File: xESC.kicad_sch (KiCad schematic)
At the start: 47 parts, among them J18 Conn_01x05, J22 Screw_Terminal_01x03, J36 Conn_02x03_Odd_Even, J39 Screw_Terminal_01x02, J42 Conn_01x02, U10 xESC2, U20 2.54mm 2x2 socket, U23 2.54mm 2x2 socket, U26 2.54mm 2x2 socket, U28 LV2862XDDC, U32 2.54mm 1x6 socket, U35 2.54mm 1x6 socket, U38 2.54mm 1x9 socket, U41 2.54mm 1x5 socket

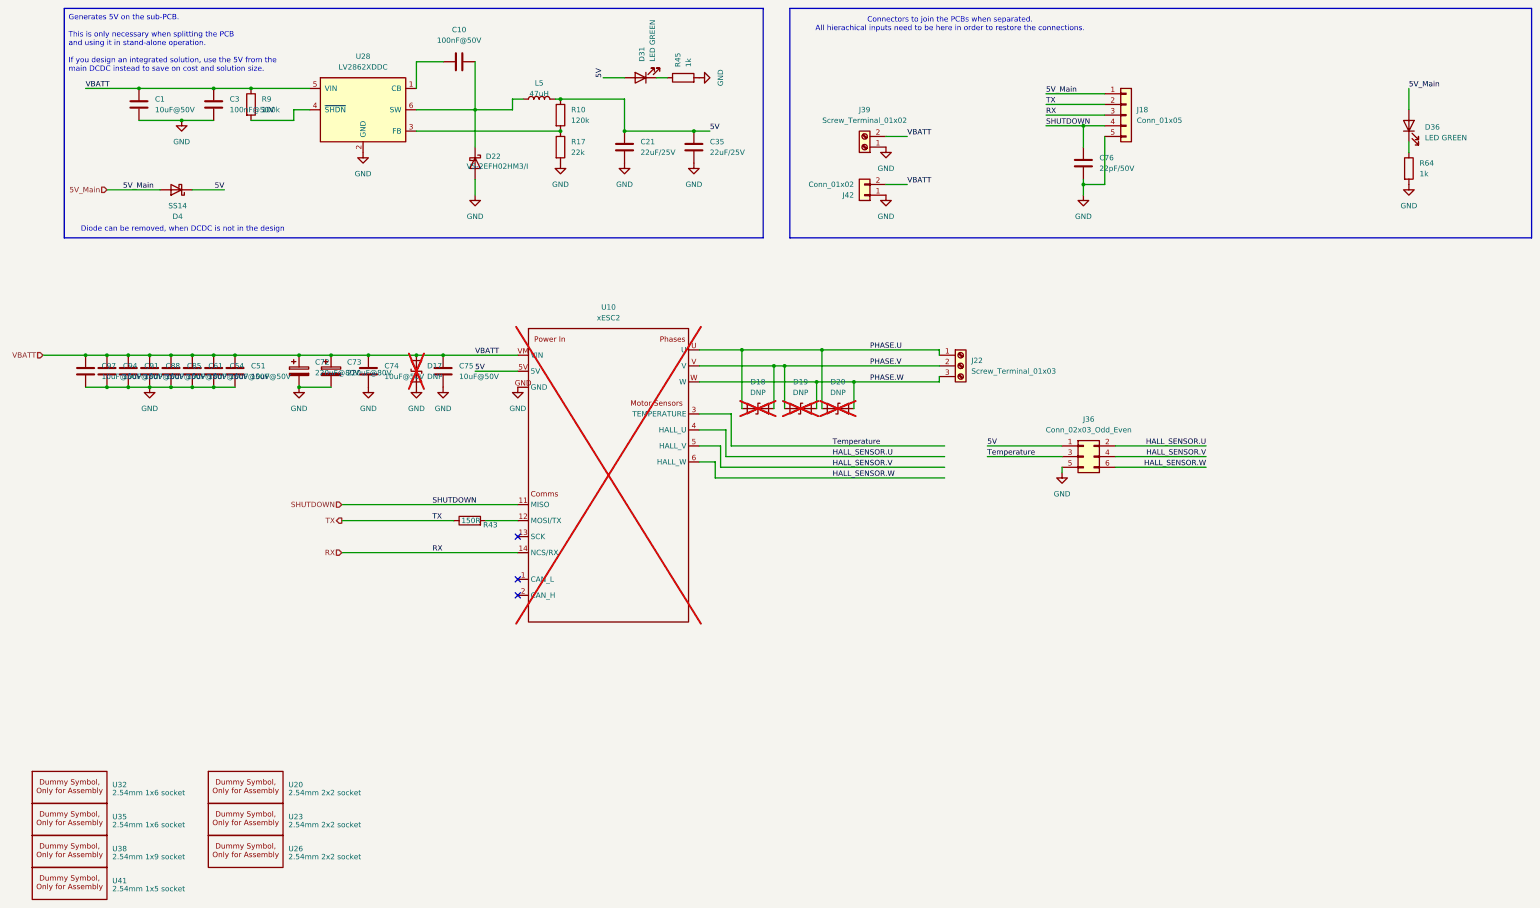
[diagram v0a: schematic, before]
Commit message: New conns for xESC
Added new connectors into the design for motors.
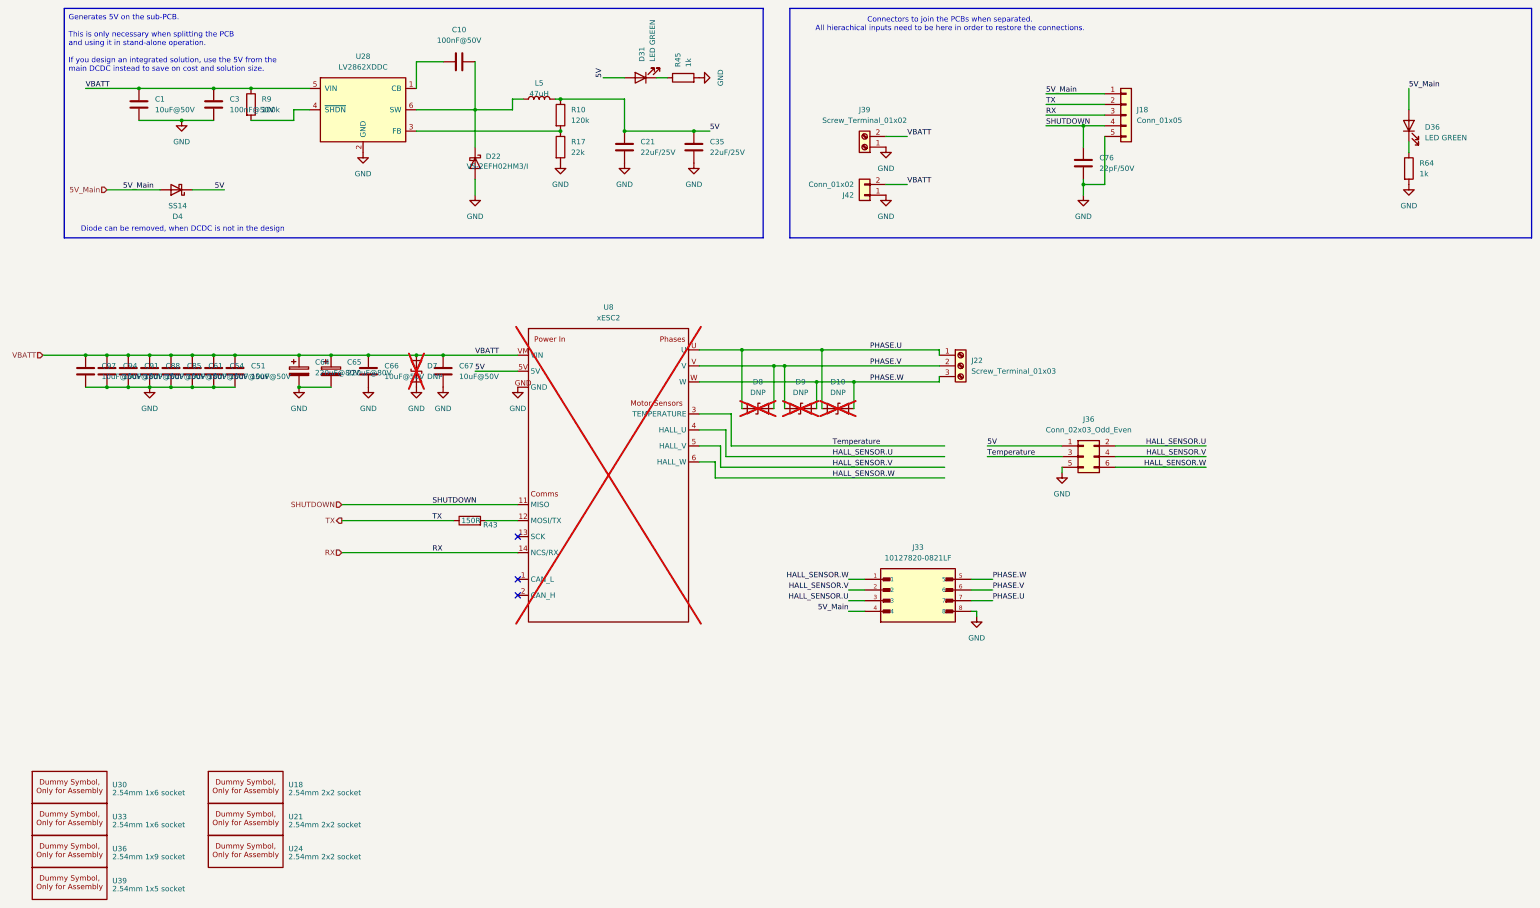
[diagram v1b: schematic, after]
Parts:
- added J33: 10127820-0821LF, 10127820_0821LF:AMPHENOL_10127820-0821LF, symbol 10127820-0821LF:10127820-0821LF
- D22: value VS-2EFH02HM3/I -> VS-2EFH02HM3/I
- renumbered C72 to C64, C73 to C65, C74 to C66, C75 to C67, D20 to D10, D17 to D7, D18 to D8, D19 to D9, U20 to U18, U23 to U21, U26 to U24, U32 to U30, U35 to U33, U38 to U36, U41 to U39, U10 to U8
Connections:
- net 5V_Main: now also J33.4
- net GND: now also J33.8
- net HALL_SENSOR.U: now also J33.3
- net HALL_SENSOR.V: now also J33.2
- net HALL_SENSOR.W: now also J33.1
- net PHASE.U: now also J33.7
- net PHASE.V: now also J33.6
- net PHASE.W: now also J33.5

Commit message: Incremental routing updates
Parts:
- removed J18: Conn_01x05, Connector_JST:JST_XH_B5B-XH-A_1x05_P2.50mm_Vertical, symbol Connector_Generic:Conn_01x05
- removed J39: Screw_Terminal_01x02, TerminalBlock_Phoenix:TerminalBlock_Phoenix_MKDS-1,5-2-5.08_1x02_P5.08mm_Horizontal, symbol Connector:Screw_Terminal_01x02
- removed J42: Conn_01x02, Connector_AMASS:AMASS_XT30U-M_1x02_P5.0mm_Vertical, symbol Connector_Generic:Conn_01x02

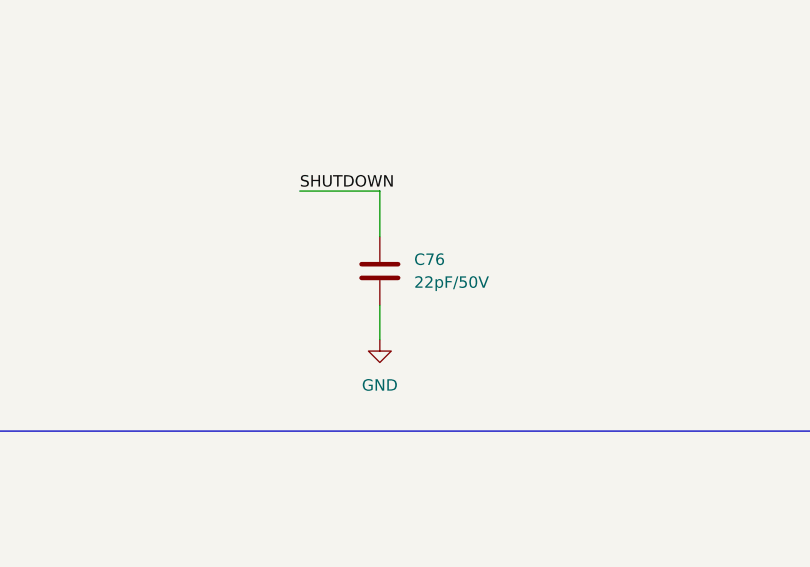
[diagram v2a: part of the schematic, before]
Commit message: Additional routing
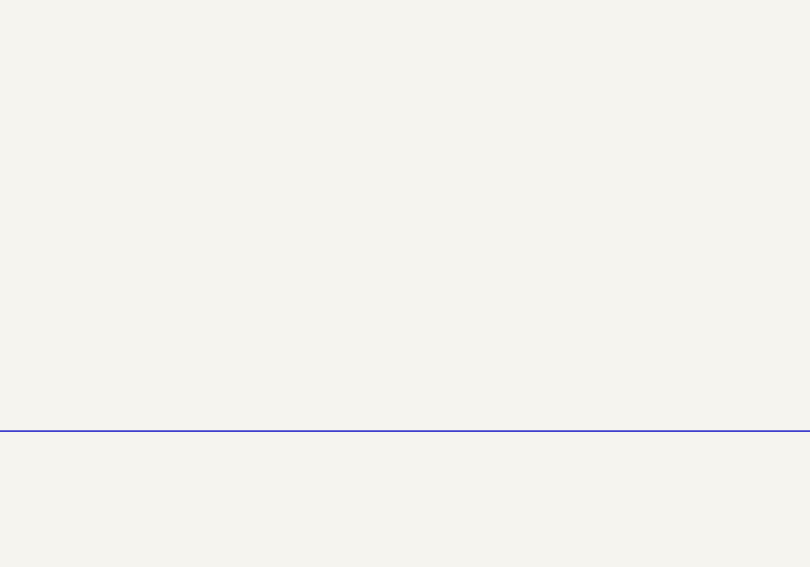
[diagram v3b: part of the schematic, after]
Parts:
- removed C76: 22pF/50V, Capacitor_SMD:C_0603_1608Metric, symbol Device:C

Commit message: Routing progress
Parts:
- D4: now not fitted
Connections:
- net 5V is gone; now on net 5V_Main: C21.1, C35.1, D31.2 (A), D4.1 (K), J36.1 (Pin_1), L5.2, R10.1, U8.5V
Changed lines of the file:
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@@
+	)
+	(junction
+		(at 57.15 60.96)
+		(diameter 0)
+		(color 0 0 0 0)
 	)
 	(junction
@@
 	(junction
 		(at 78.74 36.83)
+		(diameter 0)
+		(color 0 0 0 0)
+	)
+	(junction
+		(at 66.04 60.96)
 		(diameter 0)
 		(color 0 0 0 0)
@@
 	(wire
 		(pts
-			(xy 72.39 60.96) (xy 64.77 60.96)
+			(xy 72.39 60.96) (xy 66.04 60.96)
 		)
 		(stroke
@@
 	(wire
 		(pts
+			(xy 66.04 60.96) (xy 64.77 60.96)
+		)
+		(stroke
+			(width 0)
+			(type default)
+		)
+	)
+	(wire
+		(pts
 			(xy 62.23 44.45) (xy 69.85 44.45)
 		)
@@
 	(wire
 		(pts
+			(xy 57.15 57.15) (xy 66.04 57.15)
+		)
+		(stroke
+			(width 0)
+			(type default)
+		)
+	)
+	(wire
+		(pts
 			(xy 185.42 99.06) (xy 195.58 99.06)
 		)
@@
 	(wire
 		(pts
+			(xy 57.15 60.96) (xy 57.15 57.15)
+		)
+		(stroke
+			(width 0)
+			(type default)
+		)
+	)
+	(wire
+		(pts
 			(xy 132.08 41.91) (xy 132.08 50.8)
 		)
@@
 		(pts
 			(xy 140.97 39.37) (xy 143.51 39.37)
+		)
+		(stroke
+			(width 0)
+			(type default)
+		)
+	)
+	(wire
+		(pts
+			(xy 66.04 57.15) (xy 66.04 60.96)
 		)
 		(stroke
@@
 		(in_bom yes)
 		(on_board yes)
-		(dnp no)
+		(dnp yes)
 		(fields_autoplaced yes)
 		(property "Reference" "D4"

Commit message: Further routing progress
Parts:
- removed D31: LED GREEN, LED_SMD:LED_0805_2012Metric, symbol Device:LED
- removed J22: Screw_Terminal_01x03, TerminalBlock_Phoenix:TerminalBlock_Phoenix_MKDS-1,5-3-5.08_1x03_P5.08mm_Horizontal, symbol Connector:Screw_Terminal_01x03
- removed R45: 1k, Resistor_SMD:R_0805_2012Metric, symbol Device:R

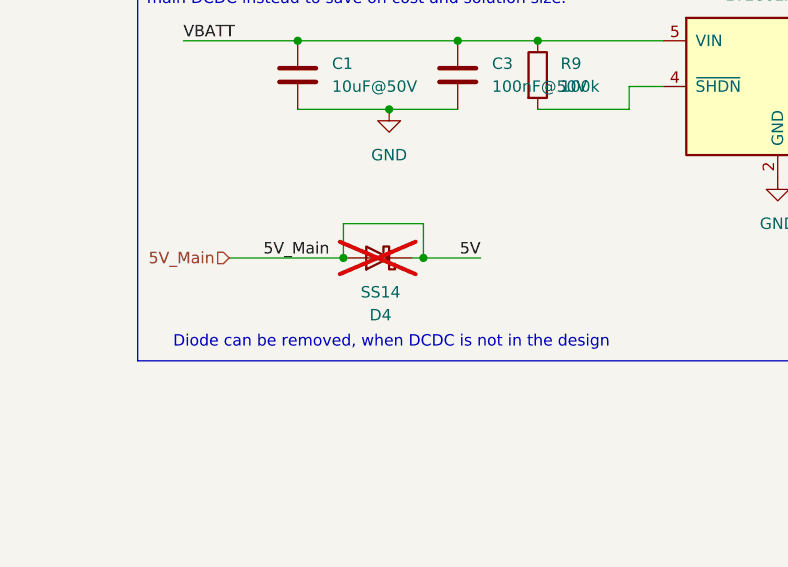
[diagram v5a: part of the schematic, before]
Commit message: Review ready layout
DRC mostly clean.  Need to add GND via stitching and GND return vias yet, and general review
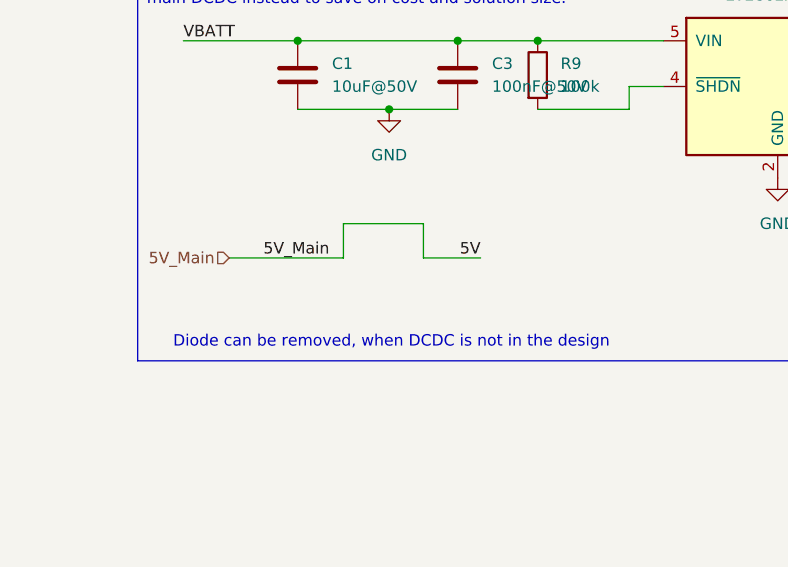
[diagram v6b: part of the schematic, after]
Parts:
- removed D4: SS14, Diode_SMD:D_SMA, symbol Diode:SS14
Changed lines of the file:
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@@
-	)
-	(junction
-		(at 57.15 60.96)
-		(diameter 0)
-		(color 0 0 0 0)
 	)
 	(junction
@@
 	(junction
 		(at 78.74 36.83)
-		(diameter 0)
-		(color 0 0 0 0)
-	)
-	(junction
-		(at 66.04 60.96)
 		(diameter 0)
 		(color 0 0 0 0)
@@
 		(pts
 			(xy 140.97 41.91) (xy 132.08 41.91)
-		)
-		(stroke
-			(width 0)
-			(type default)
-		)
-	)
-	(wire
-		(pts
-			(xy 66.04 60.96) (xy 64.77 60.96)
 		)
 		(stroke
@@
 					(unit 1)
 				)
-			)
-		)
-	)
-	(symbol
-		(lib_id "Diode:SS14")
-		(at 60.96 60.96 180)
-		(unit 1)
-		(exclude_from_sim no)
-		(in_bom yes)
-		(on_board yes)
-		(dnp yes)
-		(fields_autoplaced yes)
-		(property "Reference" "D4"
-			(at 61.2775 67.31 0)
-			(effects
-				(font
-					(size 1.27 1.27)
-				)
-			)
-		)
-		(property "Value" "SS14"
-			(at 61.2775 64.77 0)
-			(effects
-				(font
-					(size 1.27 1.27)
-				)
-			)
-		)
-		(property "Footprint" "Diode_SMD:D_SMA"
-			(at 60.96 56.515 0)
-			(effects
-				(font
-					(size 1.27 1.27)
-				)
-				(hide yes)
-			)
-		)
-		(property "Datasheet" "https://www.vishay.com/docs/88746/ss12.pdf"
-			(at 60.96 60.96 0)
-			(effects
-				(font
-					(size 1.27 1.27)
-				)
-				(hide yes)
-			)
-		)
-		(property "Description" "40V 1A Schottky Diode, SMA"
-			(at 60.96 60.96 0)
-			(effects
-				(font
-					(size 1.27 1.27)
-				)
-				(hide yes)
-			)
-		)
-		(property "Field4" ""
-			(at 60.96 60.96 0)
-			(effects
-				(font
-					(size 1.27 1.27)
-				)
-				(hide yes)
-			)
-		)
-		(property "Field5" ""
-			(at 60.96 60.96 0)
-			(effects
-				(font
-					(size 1.27 1.27)
-				)
-				(hide yes)
-			)
-		)
-		(property "Field6" ""
-			(at 60.96 60.96 0)
-			(effects
-				(font
-					(size 1.27 1.27)
-				)
-				(hide yes)
-			)
-		)
-		(property "Field7" ""
-			(at 60.96 60.96 0)
-			(effects
-				(font
-					(size 1.27 1.27)
-				)
-				(hide yes)
-			)
-		)
-		(property "JLC" "C2480"
-			(at 60.96 60.96 0)
-			(effects
-				(font
-					(size 1.27 1.27)
-				)
-				(hide yes)
-			)
-		)
-		(property "Part Description" ""
-			(at 60.96 60.96 0)
-			(effects
-				(font
-					(size 1.27 1.27)
-				)
-				(hide yes)
-			)
-		)
-		(property "Height" ""
-			(at 60.96 60.96 0)
-			(effects
-				(font
-					(size 1.27 1.27)
-				)
-				(hide yes)
-			)
-		)
-		(property "Manufacturer_Name" ""
-			(at 60.96 60.96 0)
-			(effects
-				(font
-					(size 1.27 1.27)
-				)
-				(hide yes)
-			)
-		)
-		(property "Manufacturer_Part_Number" ""
-			(at 60.96 60.96 0)
-			(effects
-				(font
-					(size 1.27 1.27)
-				)
-				(hide yes)
-			)
-		)
-		(property "Mouser Part Number" ""
-			(at 60.96 60.96 0)
-			(effects
-				(font
-					(size 1.27 1.27)
-				)
-				(hide yes)
-			)
-		)
-		(property "Mouser Price/Stock" ""
-			(at 60.96 60.96 0)
-			(effects
-				(font
-					(size 1.27 1.27)
-				)
-				(hide yes)
-			)
-		)
-		(pin "2"
-		)
-		(pin "1"
-		)
-		(instances
-			(project "hw-openmower-universal"
-				(path "/e12e8a63-1d1b-4736-9aba-a87a258b2b11/0359b790-c26c-4759-a59f-5a6b50a14036"
-					(reference "D28")
-					(unit 1)
-				)
-				(path "/e12e8a63-1d1b-4736-9aba-a87a258b2b11/2dcb05ea-788f-4ed6-923e-0b0051e68de3"
-					(reference "D4")
-					(unit 1)
-				)
